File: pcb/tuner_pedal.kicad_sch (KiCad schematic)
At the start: 54 parts, among them J1 SWD, J2 Fermion 1.8" TFT LCD, J3 UART, SW1 SW_Push, SW2 SW_Push, U1 STM32F411CEUx, U2 PCM1802DB, U3 MCP1700T-3302E/TT, U4 TPS54302, X1 ECS-2520MVLC-081.92, Y1 25MHz 9pF

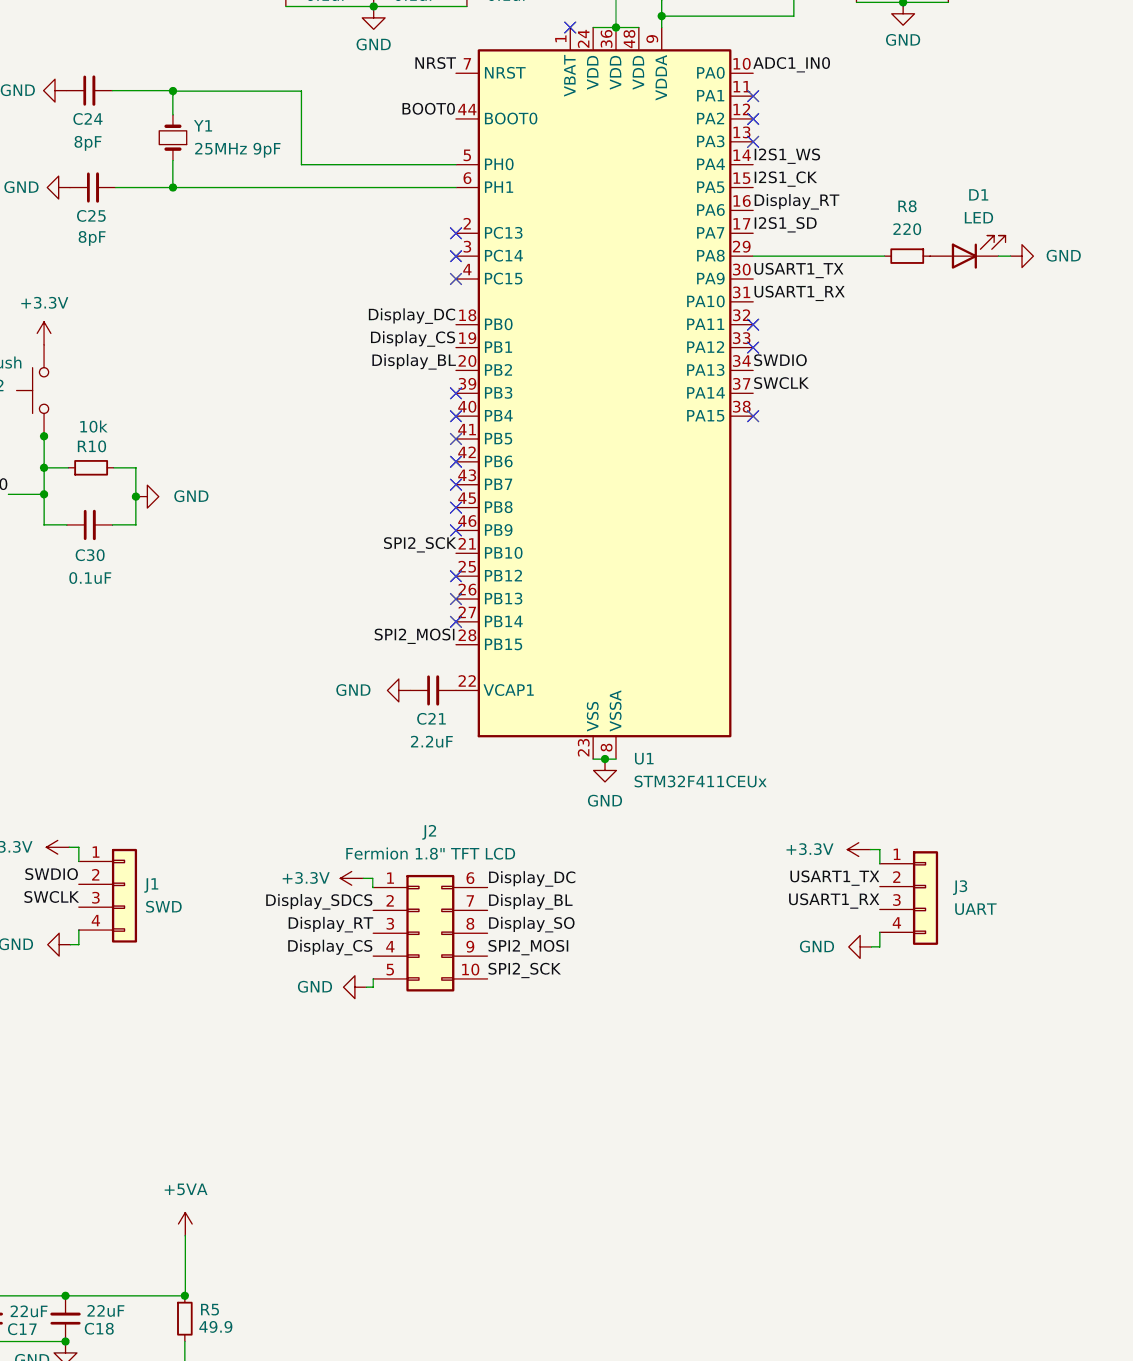
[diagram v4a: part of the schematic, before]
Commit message: Added pull-ups/downs and series termination to LCD
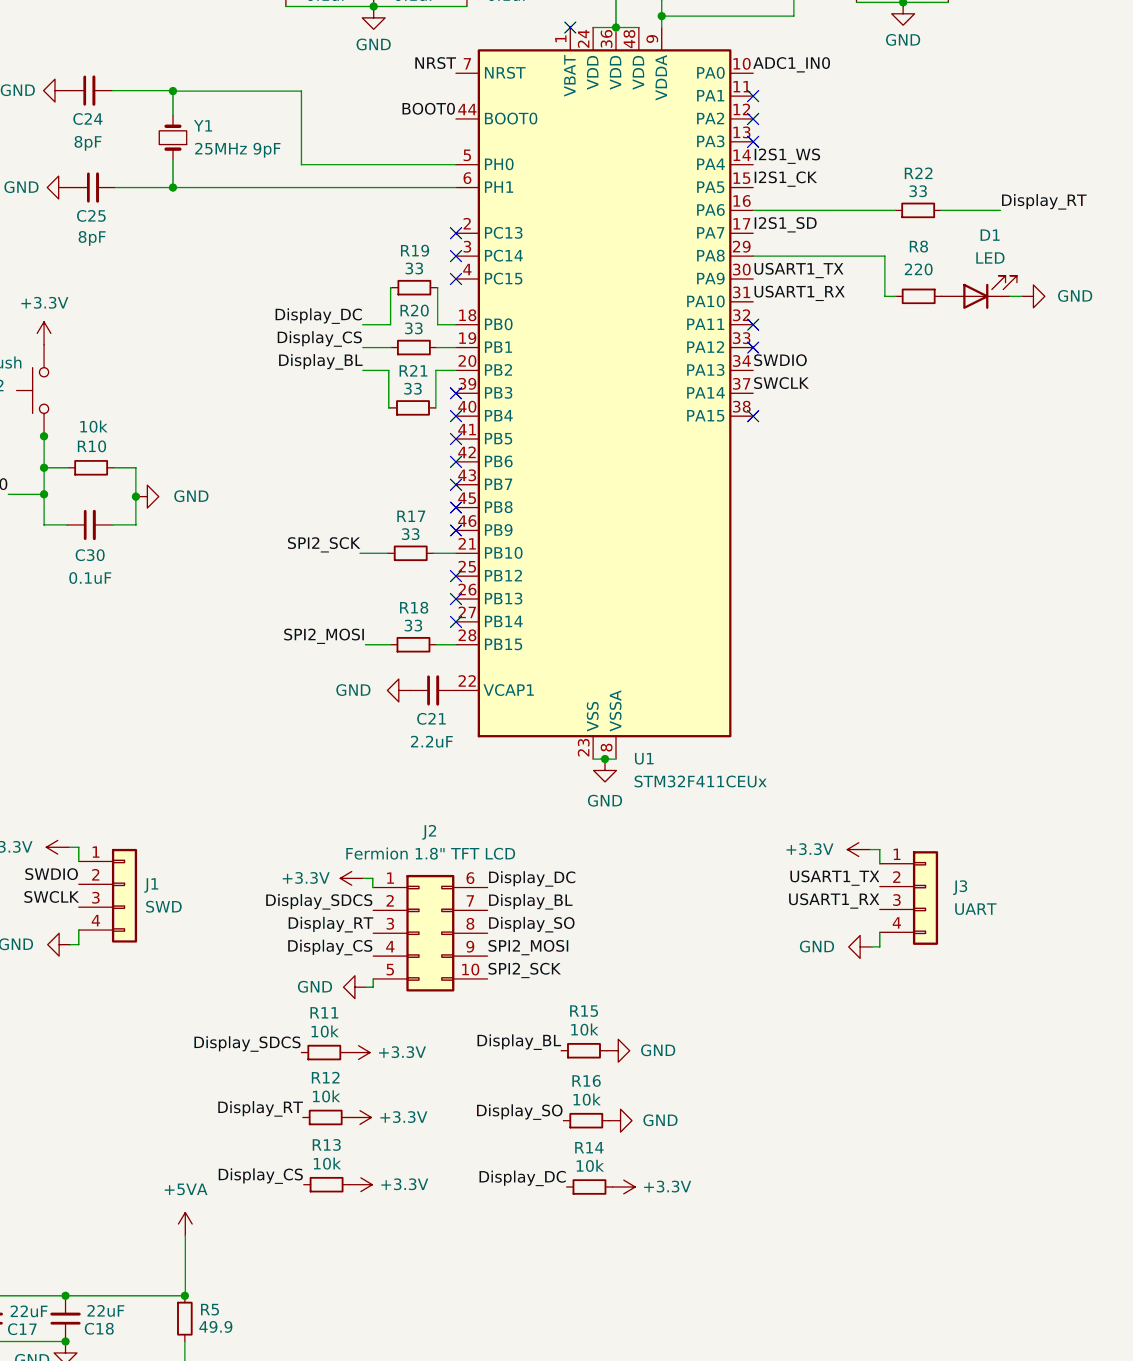
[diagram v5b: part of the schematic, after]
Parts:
- added R11, R12, R13, R14, R15, R16: 10k, symbol Device:R_Small
- added R17, R18, R19, R20, R21, R22: 33, symbol Device:R_Small
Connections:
- net +3.3V: now also R11.2, R12.2, R13.2, R14.2
- net Display_BL: now also R15.1, R21.1; no longer U1.20 (PB2)
- net Display_CS: now also R13.1, R20.1; no longer U1.19 (PB1)
- net Display_DC: now also R14.1, R19.1; no longer U1.18 (PB0)
- net Display_RT: now also R12.1, R22.2; no longer U1.16 (PA6)
- net Display_SDCS: now also R11.1
- net Display_SO: now also R16.1
- net GND: now also R15.2, R16.2
- net SPI2_MOSI: now also R18.1; no longer U1.28 (PB15)
- net SPI2_SCK: now also R17.1; no longer U1.21 (PB10)
- new net: R20.2, U1.19 (PB1)
- new net: R18.2, U1.28 (PB15)
- new net: R17.2, U1.21 (PB10)
- new net: R21.2, U1.20 (PB2)
- new net: R22.1, U1.16 (PA6)
- new net: R19.2, U1.18 (PB0)
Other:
- moved on the sheet: D1, R8

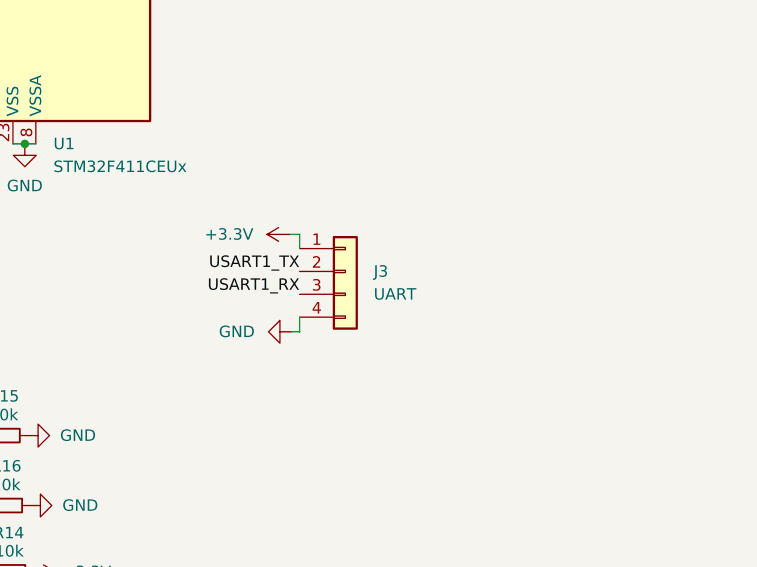
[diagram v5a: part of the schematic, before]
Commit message: Added pot pins
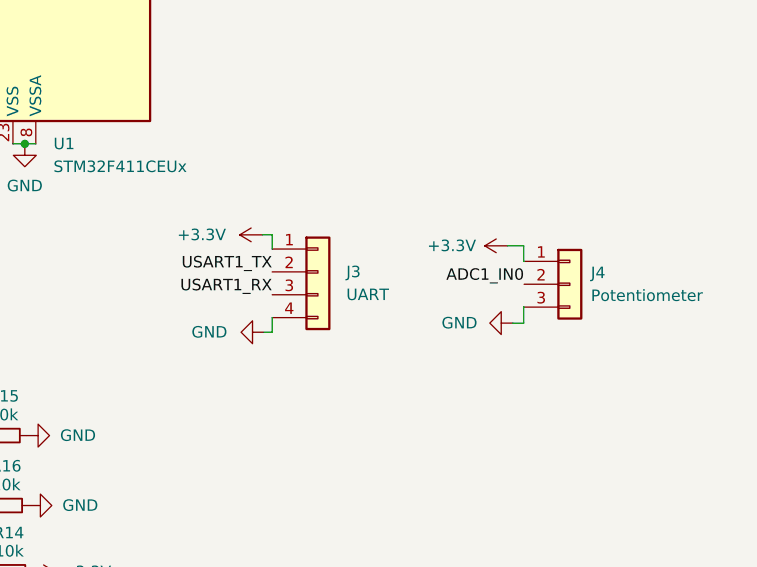
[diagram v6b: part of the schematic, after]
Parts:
- added J4: Potentiometer, Connector_PinSocket_2.54mm:PinSocket_1x03_P2.54mm_Vertical, symbol Connector_Generic:Conn_01x03
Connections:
- net +3.3V: now also J4.1 (Pin_1)
- net ADC1_IN0: now also J4.2 (Pin_2)
- net GND: now also J4.3 (Pin_3)
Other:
- moved on the sheet: J3
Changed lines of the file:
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@@
     (stroke (width 0) (type default))
   )
+  (wire (pts (xy 263.0424 128.27) (xy 263.0424 126.492))
+    (stroke (width 0) (type default))
+  )
   (wire (pts (xy 114.9096 81.28) (xy 112.3696 81.28))
     (stroke (width 0) (type default))
@@
     (stroke (width 0) (type default))
   )
+  (wire (pts (xy 261.2644 119.6848) (xy 263.0424 119.6848))
+    (stroke (width 0) (type default))
+  )
   (wire (pts (xy 96.266 86.614) (xy 96.266 89.154))
     (stroke (width 0) (type default))
@@
     (stroke (width 0) (type default))
   )
-  (wire (pts (xy 238.1504 118.4148) (xy 238.1504 119.9896))
+  (wire (pts (xy 235.1024 118.4656) (xy 235.1024 120.0404))
     (stroke (width 0) (type default))
   )
@@
     (stroke (width 0) (type default))
   )
+  (wire (pts (xy 263.0424 126.492) (xy 263.0932 126.492))
+    (stroke (width 0) (type default))
+  )
   (wire (pts (xy 238.7092 56.9468) (xy 239.9284 56.9468))
     (stroke (width 0) (type default))
@@
     (stroke (width 0) (type default))
   )
+  (wire (pts (xy 263.0424 119.6848) (xy 263.0424 121.412))
+    (stroke (width 0) (type default))
+  )
   (wire (pts (xy 42.418 24.892) (xy 42.418 41.656))
     (stroke (width 0) (type default))
@@
     (stroke (width 0) (type default))
   )
-  (wire (pts (xy 238.1504 129.2352) (xy 238.1504 127.6096))
+  (wire (pts (xy 235.1024 129.286) (xy 235.1024 127.6604))
     (stroke (width 0) (type default))
   )
@@
     (stroke (width 0) (type default))
   )
+  (wire (pts (xy 263.0424 121.412) (xy 263.0932 121.412))
+    (stroke (width 0) (type default))
+  )
   (wire (pts (xy 188.8236 65.1764) (xy 191.0588 65.1764))
     (stroke (width 0) (type default))
@@
     (stroke (width 0) (type default))
   )
+  (wire (pts (xy 261.8232 128.27) (xy 263.0424 128.27))
+    (stroke (width 0) (type default))
+  )
   (wire (pts (xy 188.976 55.9816) (xy 189.0268 55.9816))
     (stroke (width 0) (type default))
@@
     (stroke (width 0) (type default))
   )
-  (wire (pts (xy 237.236 129.2352) (xy 238.1504 129.2352))
+  (wire (pts (xy 234.188 129.286) (xy 235.1024 129.286))
     (stroke (width 0) (type default))
   )
-  (wire (pts (xy 237.0836 118.4148) (xy 238.1504 118.4148))
+  (wire (pts (xy 234.0356 118.4656) (xy 235.1024 118.4656))
     (stroke (width 0) (type default))
   )
@@
     (effects (font (size 1.27 1.27)) (justify left bottom))
   )
-  (label "USART1_RX" (at 238.1504 125.0696 180) (fields_autoplaced)
+  (label "USART1_RX" (at 235.1024 125.1204 180) (fields_autoplaced)
+    (effects (font (size 1.27 1.27)) (justify right bottom))
+  )
+  (label "ADC1_IN0" (at 263.0932 123.952 180) (fields_autoplaced)
     (effects (font (size 1.27 1.27)) (justify right bottom))
   )
@@
     (effects (font (size 1.27 1.27)) (justify left bottom))
   )
-  (label "USART1_TX" (at 238.1504 122.5296 180) (fields_autoplaced)
+  (label "USART1_TX" (at 235.1024 122.5804 180) (fields_autoplaced)
     (effects (font (size 1.27 1.27)) (justify right bottom))
   )
@@
     (effects (font (size 1.27 1.27)) (justify left bottom))
   )
+  (symbol (lib_id "power:+3.3V") (at 261.2644 119.6848 90) (unit 1)
+    (in_bom yes) (on_board yes) (dnp no) (fields_autoplaced)
+    (property "Reference" "#PWR052" (at 265.0744 119.6848 0)
+      (effects (font (size 1.27 1.27)) hide)
+    )
+    (property "Value" "+3.3V" (at 257.7592 119.6848 90)
+      (effects (font (size 1.27 1.27)) (justify left))
+    )
+    (property "Footprint" "" (at 261.2644 119.6848 0)
+      (effects (font (size 1.27 1.27)) hide)
+    )
+    (property "Datasheet" "" (at 261.2644 119.6848 0)
+      (effects (font (size 1.27 1.27)) hide)
+    )
+    (pin "1")
+    (instances
+      (project "tuner_pedal"
+        (path "/be09f3cc-c79c-49de-93a4-4a01bf6bfbcf"
+          (reference "#PWR052") (unit 1)
+        )
+      )
+    )
+  )
   (symbol (lib_id "power:+5VA") (at 97.0788 115.062 0) (unit 1)
     (in_bom yes) (on_board yes) (dnp no) (fields_autoplaced)
@@
     )
   )
-  (symbol (lib_id "power:GND") (at 237.236 129.2352 270) (unit 1)
+  (symbol (lib_id "power:GND") (at 234.188 129.286 270) (unit 1)
     (in_bom yes) (on_board yes) (dnp no) (fields_autoplaced)
-    (property "Reference" "#PWR039" (at 230.886 129.2352 0)
+    (property "Reference" "#PWR039" (at 227.838 129.286 0)
       (effects (font (size 1.27 1.27)) hide)
     )
-    (property "Value" "GND" (at 233.172 129.2352 90)
+    (property "Value" "GND" (at 230.124 129.286 90)
       (effects (font (size 1.27 1.27)) (justify right))
     )
-    (property "Footprint" "" (at 237.236 129.2352 0)
+    (property "Footprint" "" (at 234.188 129.286 0)
       (effects (font (size 1.27 1.27)) hide)
     )
-    (property "Datasheet" "" (at 237.236 129.2352 0)
+    (property "Datasheet" "" (at 234.188 129.286 0)
       (effects (font (size 1.27 1.27)) hide)
     )
@@
     )
   )
-  (symbol (lib_id "Connector_Generic:Conn_01x04") (at 243.2304 122.5296 0) (unit 1)
+  (symbol (lib_id "Connector_Generic:Conn_01x04") (at 240.1824 122.5804 0) (unit 1)
     (in_bom yes) (on_board yes) (dnp no) (fields_autoplaced)
-    (property "Reference" "J3" (at 246.38 122.5296 0)
+    (property "Reference" "J3" (at 243.332 122.5804 0)
       (effects (font (size 1.27 1.27)) (justify left))
     )
-    (property "Value" "UART" (at 246.38 125.0696 0)
+    (property "Value" "UART" (at 243.332 125.1204 0)
       (effects (font (size 1.27 1.27)) (justify left))
     )
-    (property "Footprint" "Connector_PinHeader_2.54mm:PinHeader_1x04_P2.54mm_Vertical" (at 243.2304 122.5296 0)
+    (property "Footprint" "Connector_PinHeader_2.54mm:PinHeader_1x04_P2.54mm_Vertical" (at 240.1824 122.5804 0)
       (effects (font (size 1.27 1.27)) hide)
     )
-    (property "Datasheet" "~" (at 243.2304 122.5296 0)
+    (property "Datasheet" "~" (at 240.1824 122.5804 0)
       (effects (font (size 1.27 1.27)) hide)
     )
@@
     )
   )
+  (symbol (lib_id "Connector_Generic:Conn_01x03") (at 268.1732 123.952 0) (unit 1)
+    (in_bom yes) (on_board yes) (dnp no) (fields_autoplaced)
+    (property "Reference" "J4" (at 270.51 122.682 0)
+      (effects (font (size 1.27 1.27)) (justify left))
+    )
+    (property "Value" "Potentiometer" (at 270.51 125.222 0)
+      (effects (font (size 1.27 1.27)) (justify left))
+    )
+    (property "Footprint" "Connector_PinSocket_2.54mm:PinSocket_1x03_P2.54mm_Vertical" (at 268.1732 123.952 0)
+      (effects (font (size 1.27 1.27)) hide)
+    )
+    (property "Datasheet" "~" (at 268.1732 123.952 0)
+      (effects (font (size 1.27 1.27)) hide)
+    )
+    (pin "1")
+    (pin "2")
+    (pin "3")
+    (instances
+      (project "tuner_pedal"
+        (path "/be09f3cc-c79c-49de-93a4-4a01bf6bfbcf"
+          (reference "J4") (unit 1)
+        )
+      )
+    )
+  )
   (symbol (lib_id "Device:R_Small") (at 160.9344 179.2224 0) (unit 1)
     (in_bom yes) (on_board yes) (dnp no)
@@
     )
   )
-  (symbol (lib_id "power:+3.3V") (at 237.0836 118.4148 90) (unit 1)
+  (symbol (lib_id "power:+3.3V") (at 234.0356 118.4656 90) (unit 1)
     (in_bom yes) (on_board yes) (dnp no) (fields_autoplaced)
-    (property "Reference" "#PWR038" (at 240.8936 118.4148 0)
+    (property "Reference" "#PWR038" (at 237.8456 118.4656 0)
       (effects (font (size 1.27 1.27)) hide)
     )
-    (property "Value" "+3.3V" (at 233.0196 118.4148 90)
+    (property "Value" "+3.3V" (at 229.9716 118.4656 90)
       (effects (font (size 1.27 1.27)) (justify left))
     )
-    (property "Footprint" "" (at 237.0836 118.4148 0)
+    (property "Footprint" "" (at 234.0356 118.4656 0)
       (effects (font (size 1.27 1.27)) hide)
     )
-    (property "Datasheet" "" (at 237.0836 118.4148 0)
+    (property "Datasheet" "" (at 234.0356 118.4656 0)
       (effects (font (size 1.27 1.27)) hide)
     )
@@
         )
       )
+    )
+  )
+  (symbol (lib_id "power:GND") (at 261.8232 128.27 270) (unit 1)
+    (in_bom yes) (on_board yes) (dnp no) (fields_autoplaced)
+    (property "Reference" "#PWR051" (at 255.4732 128.27 0)
+      (effects (font (size 1.27 1.27)) hide)
+    )
+    (property "Value" "GND" (at 257.9116 128.27 90)
+      (effects (font (size 1.27 1.27)) (justify right))
+    )
+    (property "Footprint" "" (at 261.8232 128.27 0)
+      (effects (font (size 1.27 1.27)) hide)
+    )
+    (property "Datasheet" "" (at 261.8232 128.27 0)
+      (effects (font (size 1.27 1.27)) hide)
+    )
+    (pin "1")
+    (instances
+      (project "tuner_pedal"
+        (path "/be09f3cc-c79c-49de-93a4-4a01bf6bfbcf"
+          (reference "#PWR051") (unit 1)
+        )
+      )
